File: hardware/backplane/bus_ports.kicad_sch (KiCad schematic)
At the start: 2 parts, among them J21 FR_1,27/80-xx, J22 FR_1,27/80-xx

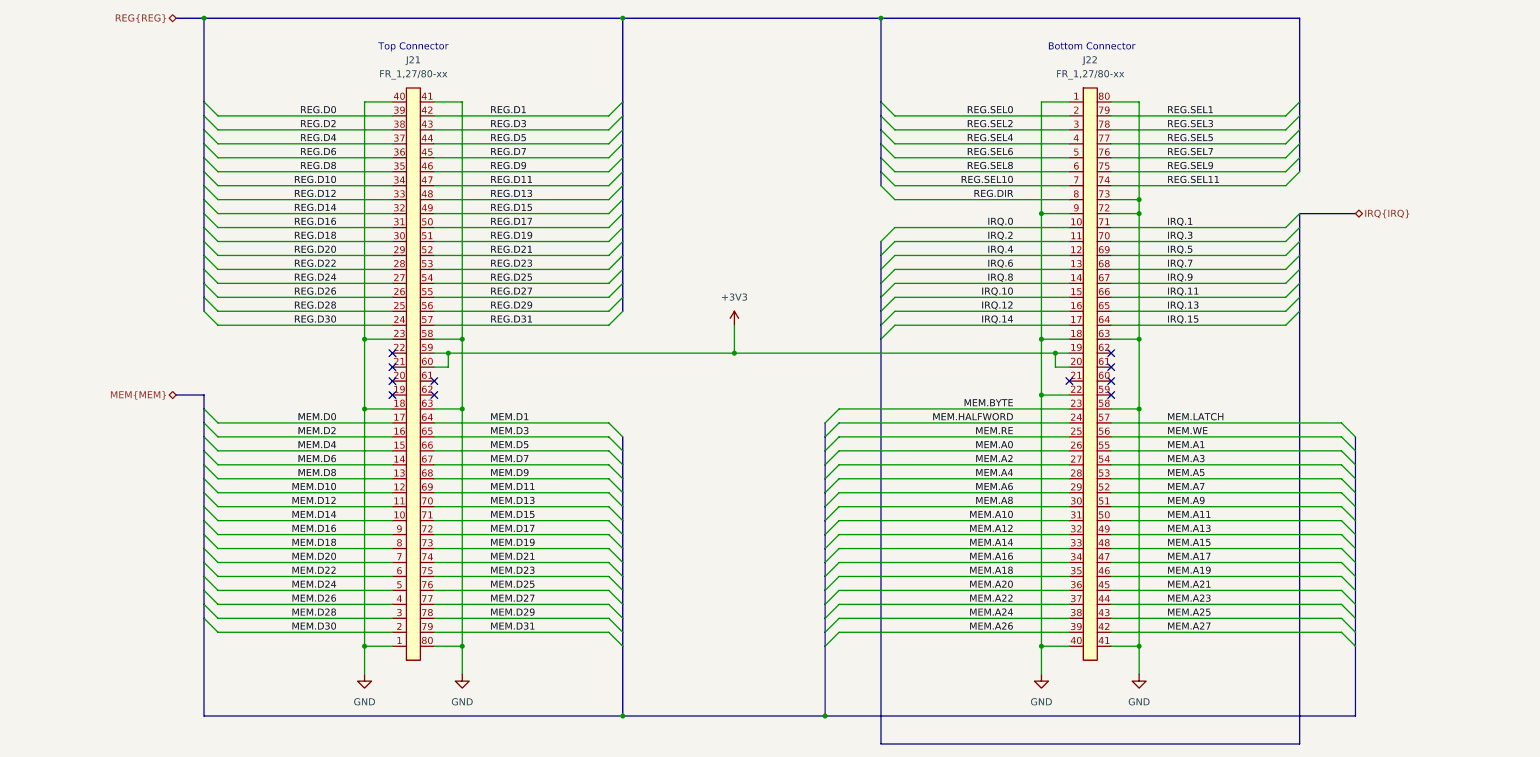
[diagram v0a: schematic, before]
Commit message: feat: Assign footprints, add testpoints
 * Verify all footprints are assigned.
 * Create testpoints for key signals.
 * Reorganize component libraries.
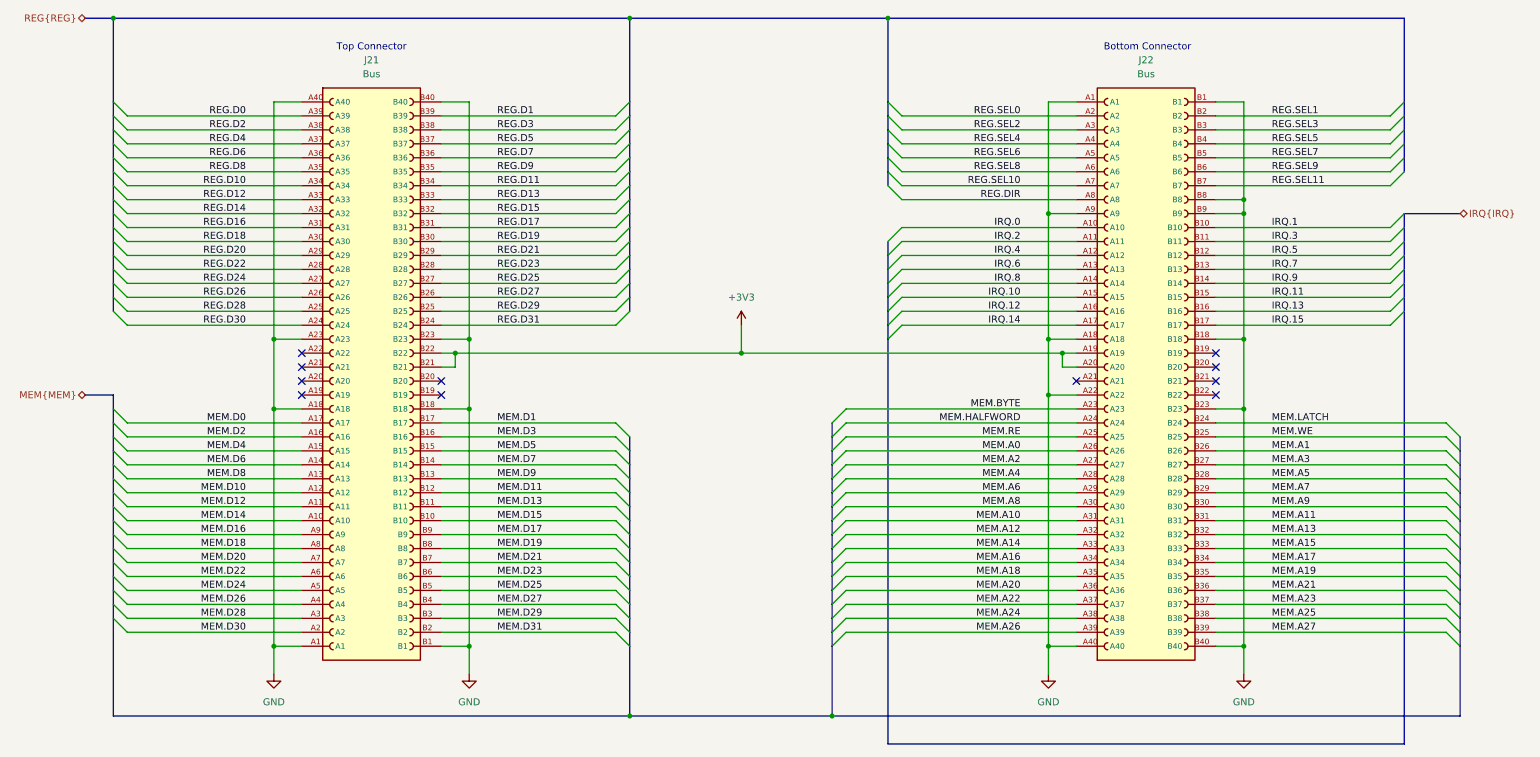
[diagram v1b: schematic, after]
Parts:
- removed J21, J22: FR_1,27/80-xx, symbol FR-1-27-80-xx:FR_1,27/80-xx
- added J21, J22: Bus, 1337020:PHOENIX_1337020, symbol 1337020:1337020
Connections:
- net +3V3: now also J21.B21, J21.B22, J22.A19, J22.A20
- net GND: now also J21.A1, J21.A18, J21.A23, J21.A40, J21.B1, J21.B18, J21.B23, J21.B40, J22.A1, J22.A18, J22.A22, J22.A40, J22.A9, J22.B1, J22.B18, J22.B23, J22.B40, J22.B8, J22.B9
- net IRQ.0: now also J22.A10
- net IRQ.1: now also J22.B10
- net IRQ.10: now also J22.A15
- net IRQ.11: now also J22.B15
- net IRQ.12: now also J22.A16
- net IRQ.13: now also J22.B16
- net IRQ.14: now also J22.A17
- net IRQ.15: now also J22.B17
- net IRQ.2: now also J22.A11
- net IRQ.3: now also J22.B11
- net IRQ.4: now also J22.A12
- net IRQ.5: now also J22.B12
- net IRQ.6: now also J22.A13
- net IRQ.7: now also J22.B13
- net IRQ.8: now also J22.A14
- net IRQ.9: now also J22.B14
- net MEM.A0: now also J22.A26
- net MEM.A1: now also J22.B26
- net MEM.A10: now also J22.A31
- net MEM.A11: now also J22.B31
- net MEM.A12: now also J22.A32
- net MEM.A13: now also J22.B32
- net MEM.A14: now also J22.A33
- net MEM.A15: now also J22.B33
- net MEM.A16: now also J22.A34
- net MEM.A17: now also J22.B34
- net MEM.A18: now also J22.A35
- net MEM.A19: now also J22.B35
- net MEM.A2: now also J22.A27
- net MEM.A20: now also J22.A36
- net MEM.A21: now also J22.B36
- net MEM.A22: now also J22.A37
- net MEM.A23: now also J22.B37
- net MEM.A24: now also J22.A38
- net MEM.A25: now also J22.B38
- net MEM.A26: now also J22.A39
- net MEM.A27: now also J22.B39
- net MEM.A3: now also J22.B27
- net MEM.A4: now also J22.A28
- net MEM.A5: now also J22.B28
- net MEM.A6: now also J22.A29
- net MEM.A7: now also J22.B29
- net MEM.A8: now also J22.A30
- net MEM.A9: now also J22.B30
- net MEM.BYTE: now also J22.A23
- net MEM.D0: now also J21.A17
- net MEM.D1: now also J21.B17
- net MEM.D10: now also J21.A12
- net MEM.D11: now also J21.B12
- net MEM.D12: now also J21.A11
- net MEM.D13: now also J21.B11
- net MEM.D14: now also J21.A10
- net MEM.D15: now also J21.B10
- net MEM.D16: now also J21.A9
- net MEM.D17: now also J21.B9
- net MEM.D18: now also J21.A8
- net MEM.D19: now also J21.B8
- net MEM.D2: now also J21.A16
- net MEM.D20: now also J21.A7
- net MEM.D21: now also J21.B7
- net MEM.D22: now also J21.A6
- net MEM.D23: now also J21.B6
- net MEM.D24: now also J21.A5
- net MEM.D25: now also J21.B5
- net MEM.D26: now also J21.A4
- net MEM.D27: now also J21.B4
- net MEM.D28: now also J21.A3
- net MEM.D29: now also J21.B3
- net MEM.D3: now also J21.B16
- net MEM.D30: now also J21.A2
- net MEM.D31: now also J21.B2
- net MEM.D4: now also J21.A15
- net MEM.D5: now also J21.B15
- net MEM.D6: now also J21.A14
- net MEM.D7: now also J21.B14
- net MEM.D8: now also J21.A13
- net MEM.D9: now also J21.B13
- net MEM.HALFWORD: now also J22.A24
- net MEM.LATCH: now also J22.B24
- net MEM.RE: now also J22.A25
- net MEM.WE: now also J22.B25
- net REG.D0: now also J21.A39
- net REG.D1: now also J21.B39
- net REG.D10: now also J21.A34
- net REG.D11: now also J21.B34
- net REG.D12: now also J21.A33
- net REG.D13: now also J21.B33
- net REG.D14: now also J21.A32
- net REG.D15: now also J21.B32
- net REG.D16: now also J21.A31
- net REG.D17: now also J21.B31
- net REG.D18: now also J21.A30
- net REG.D19: now also J21.B30
- net REG.D2: now also J21.A38
- net REG.D20: now also J21.A29
- net REG.D21: now also J21.B29
- net REG.D22: now also J21.A28
- net REG.D23: now also J21.B28
- net REG.D24: now also J21.A27
- net REG.D25: now also J21.B27
- net REG.D26: now also J21.A26
- net REG.D27: now also J21.B26
- net REG.D28: now also J21.A25
- net REG.D29: now also J21.B25
- net REG.D3: now also J21.B38
- net REG.D30: now also J21.A24
- net REG.D31: now also J21.B24
- net REG.D4: now also J21.A37
- net REG.D5: now also J21.B37
- net REG.D6: now also J21.A36
- net REG.D7: now also J21.B36
- net REG.D8: now also J21.A35
- net REG.D9: now also J21.B35
- net REG.DIR: now also J22.A8
- net REG.SEL0: now also J22.A2
- net REG.SEL1: now also J22.B2
- net REG.SEL10: now also J22.A7
- net REG.SEL11: now also J22.B7
- net REG.SEL2: now also J22.A3
- net REG.SEL3: now also J22.B3
- net REG.SEL4: now also J22.A4
- net REG.SEL5: now also J22.B4
- net REG.SEL6: now also J22.A5
- net REG.SEL7: now also J22.B5
- net REG.SEL8: now also J22.A6
- net REG.SEL9: now also J22.B6

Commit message: feat: Apply bus arch changes to backplane schematic
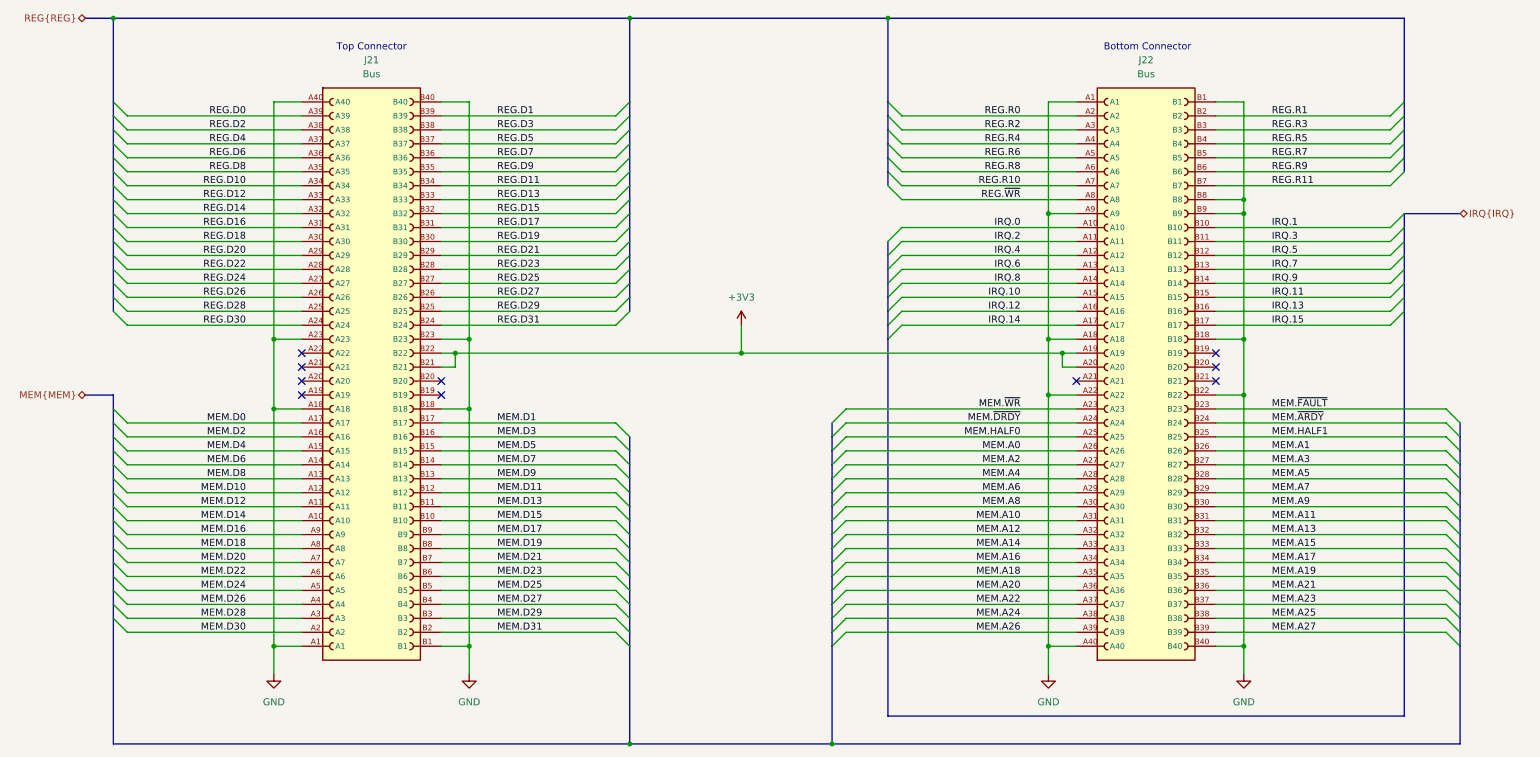
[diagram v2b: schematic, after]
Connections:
- net GND: now also J22.B22; no longer J22.B23
- net MEM.BYTE renamed MEM.~{WR}
- net MEM.HALFWORD renamed MEM.~{DRDY}
- net MEM.LATCH renamed MEM.~{ARDY}
- net MEM.RE renamed MEM.HALF0
- net MEM.WE renamed MEM.HALF1
- net REG.DIR renamed REG.~{WR}
- net REG.SEL0 renamed REG.R0
- net REG.SEL1 renamed REG.R1
- net REG.SEL10 renamed REG.R10
- net REG.SEL11 renamed REG.R11
- net REG.SEL2 renamed REG.R2
- net REG.SEL3 renamed REG.R3
- net REG.SEL4 renamed REG.R4
- net REG.SEL5 renamed REG.R5
- net REG.SEL6 renamed REG.R6
- net REG.SEL7 renamed REG.R7
- net REG.SEL8 renamed REG.R8
- net REG.SEL9 renamed REG.R9
- new net MEM.~{FAULT}: J22.B23
- no-connect marks 11 -> 10
